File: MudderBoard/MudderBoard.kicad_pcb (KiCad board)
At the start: 2 copper layers, 248.2 x 122.9 mm, 157 parts, among them K1 AZ2850-2A-12DE, M1 NMOS, M2 NMOS, M3 N-MOSFET, M4 N-MOSFET, Q1 CSD16327Q3, Q2 NPN, U1 LM5122QMH/NOPB, U2 TPS566242DRLR, U3 LP38691DTX-3.3/NOPB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

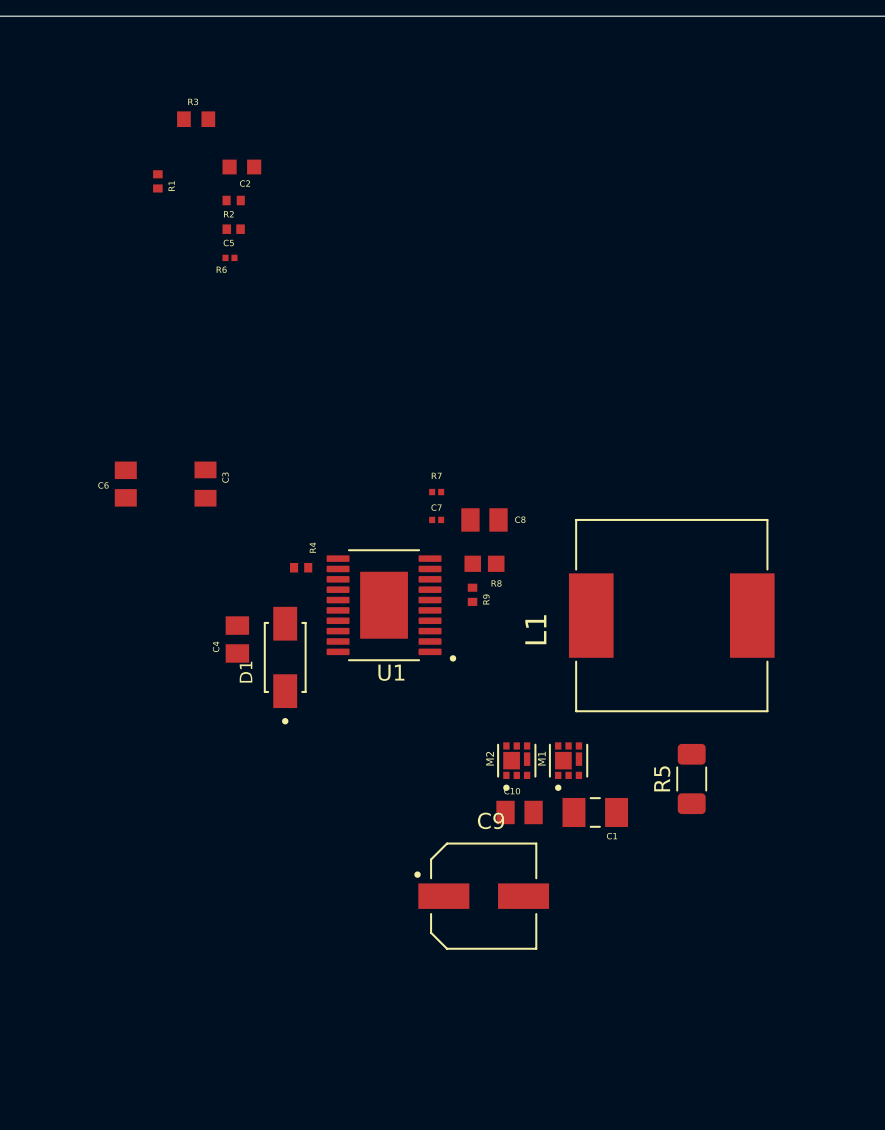
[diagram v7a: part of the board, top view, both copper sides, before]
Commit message: Layout
Final save, pixhawk and lidar
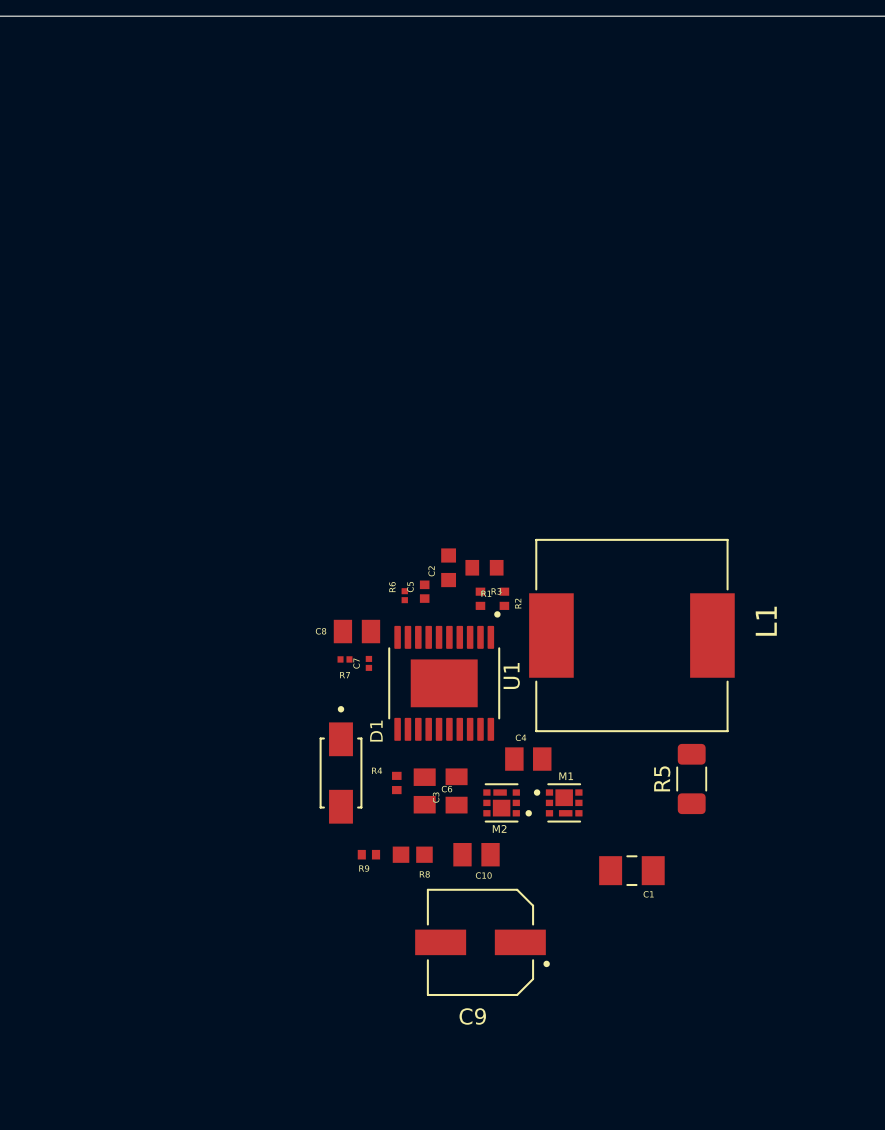
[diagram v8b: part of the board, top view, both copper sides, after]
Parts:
- moved R3 33.5 mm to (220.0, 66.0), turned to 180 degrees
- moved R1 33.1 mm to (219.8, 67.9), turned to 90 degrees
- moved R2 30.2 mm to (221.2, 67.9), turned to -90 degrees
- moved C2 28.3 mm to (217.8, 66.0), turned to 90 degrees
- moved C6 26.9 mm to (216.2, 80.0), turned to -90 degrees
- moved C5 25.7 mm to (216.2, 67.5), turned to 90 degrees
- moved C3 24.9 mm to (218.2, 80.0), turned to 90 degrees
- moved R6 23.9 mm to (215.0, 67.8), turned to 90 degrees
- moved C4 19.7 mm to (222.8, 78.0), turned to 0 degrees
- moved R8 18.8 mm to (215.5, 84.0)
- moved R9 17.6 mm to (212.8, 84.0), turned to 180 degrees
- moved R4 14.8 mm to (214.5, 79.5), turned to -90 degrees
- moved R7 12.0 mm to (211.2, 71.8), turned to 0 degrees
- moved C8 10.6 mm to (212.0, 70.0), turned to 0 degrees
- moved C7 9.95 mm to (212.8, 72.0), turned to 90 degrees
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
